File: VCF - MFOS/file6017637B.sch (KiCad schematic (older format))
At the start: 30 parts, among them J8 CV_Res, U6 TL082, U7 LM13700, U8 TL082

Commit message: VCF
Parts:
- removed J8: CV_Res, symbol Connector:AudioJack2
- added J11: XRES, symbol Connector:Conn_01x01_Female
- RV1: renamed from RV3; value R_POT_US -> 100K
- renumbered C12 to C10, C13 to C11, C14 to C12, C15 to C13, C16 to C14, C9 to C7, C10 to C8, C11 to C9, R44 to R34, R45 to R35, R46 to R36, R47 to R37, R48 to R38, R49 to R39, R50 to R40, R51 to R41, R52 to R42, R53 to R43, R54 to R44, R55 to R45, R56 to R46, R57 to R47, R58 to R48, R59 to R49, R60 to R50, U6 to U5, U7 to U6, U8 to U7
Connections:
- net at R34.1: now also J11.1 (Pin_1)

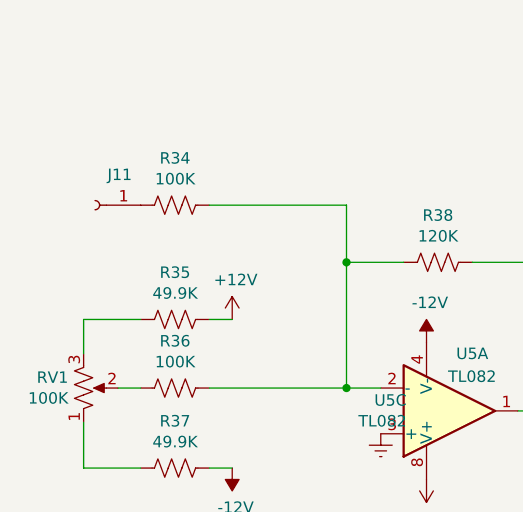
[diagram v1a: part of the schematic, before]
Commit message: fixed some incorrect component values
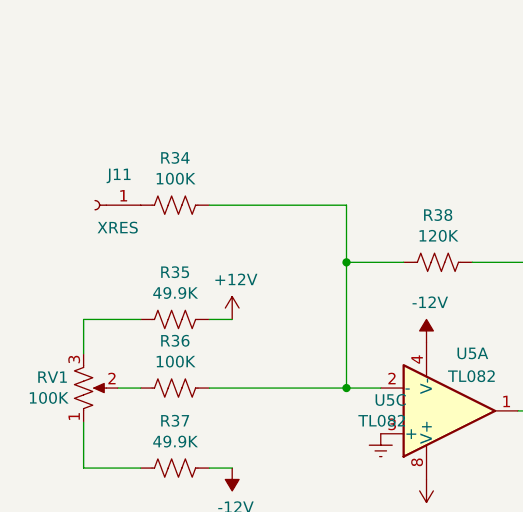
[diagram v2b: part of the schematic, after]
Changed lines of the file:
@@
 EESchema Schematic File Version 4
-EELAYER 30 0
+LIBS:VCF - MFOS-cache
+EELAYER 29 0
 EELAYER END
 $Descr A4 11693 8268
@@
 P 1300 1450
 F 0 "J11" H 1192 1317 50  0000 C CNN
-F 1 "XRES" H 1192 1316 50  0001 C CNN
+F 1 "XRES" H 1200 1550 50  0000 C CNN
 F 2 "" H 1300 1450 50  0001 C CNN
 F 3 "~" H 1300 1450 50  0001 C CNN
